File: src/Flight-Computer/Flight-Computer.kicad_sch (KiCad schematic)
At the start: 30 parts, among them J1 Jumper_NO, P8 3220-20-0200-00, U1 STM32H750VBTx, Y1 ECS-240-18-33-JGN-TR

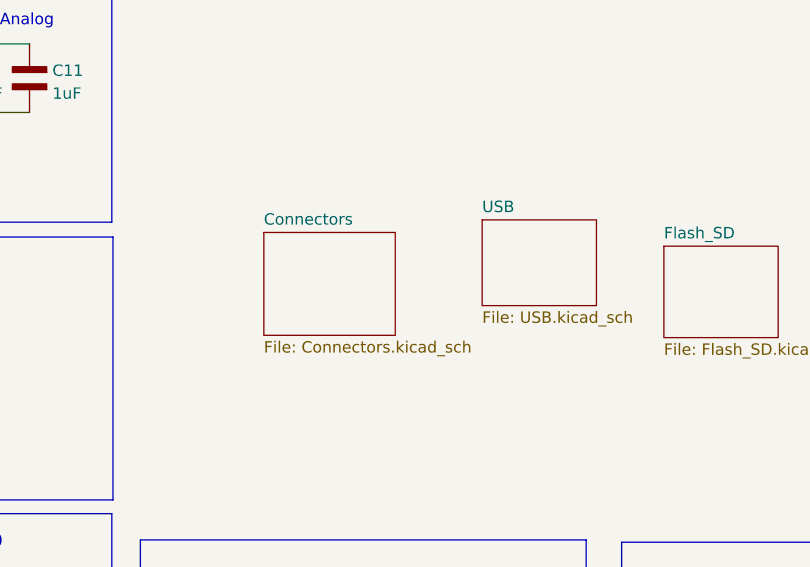
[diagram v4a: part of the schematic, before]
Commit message: deleted connector schematic sheet
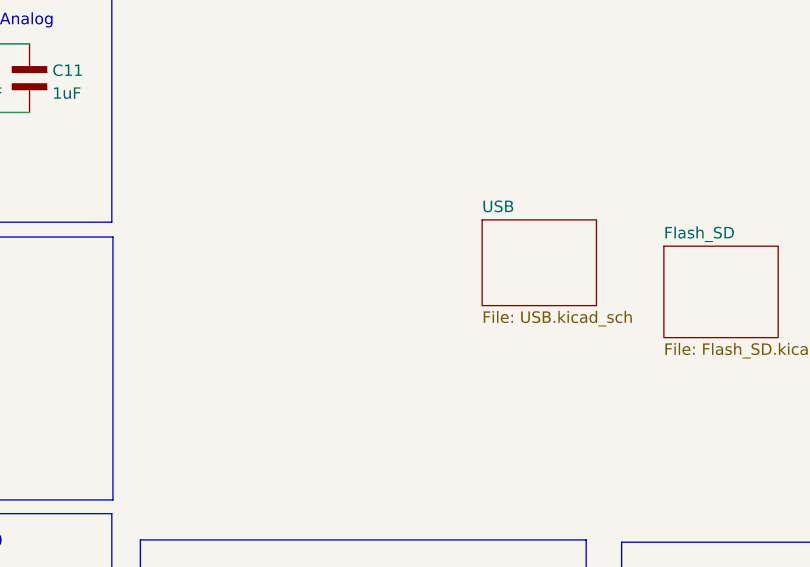
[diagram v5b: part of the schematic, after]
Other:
- removed sheet Connectors
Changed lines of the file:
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@@
-    )
-  )
-  (sheet (at 190.881 59.817) (size 14.605 11.43) (fields_autoplaced)
-    (stroke (width 0) (type solid) (color 0 0 0 0))
-    (fill (color 0 0 0 0.0000))
-    (property "Sheet name" "Connectors" (id 0) (at 190.881 59.1054 0)
-      (effects (font (size 1.27 1.27)) (justify left bottom))
-    )
-    (property "Sheet file" "Connectors.kicad_sch" (id 1) (at 190.881 71.8316 0)
-      (effects (font (size 1.27 1.27)) (justify left top))
     )
   )
@@
     (path "/" (page "1"))
     (path "/00000000-0000-0000-0000-00006177d07c" (page "3"))
-    (path "/00000000-0000-0000-0000-000060e24895" (page "4"))
     (path "/00000000-0000-0000-0000-000060daa9b3" (page "5"))
   )
@@
     (path "/00000000-0000-0000-0000-000060de602c"
       (reference "#PWR01") (unit 1) (value "Earth") (footprint "")
-    )
-    (path "/00000000-0000-0000-0000-000060e24895/00000000-0000-0000-0000-00006138d033"
-      (reference "#PWR02") (unit 1) (value "Earth") (footprint "")
     )
     (path "/00000000-0000-0000-0000-00006177d07c/00000000-0000-0000-0000-000061788b6e"
@@
     (path "/00000000-0000-0000-0000-00006177d07c/00000000-0000-0000-0000-0000617f979c"
       (reference "#PWR05") (unit 1) (value "Earth") (footprint "")
-    )
-    (path "/00000000-0000-0000-0000-000060e24895/00000000-0000-0000-0000-00006193d92b"
-      (reference "#PWR06") (unit 1) (value "Earth") (footprint "")
-    )
-    (path "/00000000-0000-0000-0000-000060e24895/00000000-0000-0000-0000-000061c08552"
-      (reference "#PWR07") (unit 1) (value "Earth") (footprint "")
     )
     (path "/08947480-7ace-467b-8a10-40dde61ef700"
@@
     (path "/00000000-0000-0000-0000-000060daa9b3/00000000-0000-0000-0000-000060fb3329"
       (reference "#PWR0110") (unit 1) (value "Earth") (footprint "")
-    )
-    (path "/00000000-0000-0000-0000-000060e24895/00000000-0000-0000-0000-000060dbde57"
-      (reference "#PWR0112") (unit 1) (value "Earth") (footprint "")
     )
     (path "/cea4c973-2fb2-41e2-9d5a-5ad0a7921ca6"
@@
       (reference "P2") (unit 1) (value "USB") (footprint "Engine-Controller:USB-TypeB")
     )
-    (path "/00000000-0000-0000-0000-000060e24895/00000000-0000-0000-0000-00006193d931"
-      (reference "P3") (unit 1) (value "SBH11-PBPC-D05-RA-BK") (footprint "Engine-Controller:SBH11-PBPC-D05-RA-BK")
-    )
-    (path "/00000000-0000-0000-0000-000060e24895/00000000-0000-0000-0000-000061252cb3"
-      (reference "P4") (unit 1) (value "0901471110") (footprint "Engine-Controller:0901471110")
-    )
-    (path "/00000000-0000-0000-0000-000060e24895/00000000-0000-0000-0000-000061255d75"
-      (reference "P5") (unit 1) (value "66953-005LF") (footprint "Engine-Controller:66953-005LF")
-    )
     (path "/00000000-0000-0000-0000-00006177d07c/00000000-0000-0000-0000-0000617f7ccb"
       (reference "P6") (unit 1) (value "Micro_SD_Card") (footprint "Engine-Controller:GCT_MEM2075-00-140-01-A")
-    )
-    (path "/00000000-0000-0000-0000-000060e24895/00000000-0000-0000-0000-000061bf9e85"
-      (reference "P7") (unit 1) (value "0901471110") (footprint "Engine-Controller:0901471110")
     )
     (path "/b101f496-de41-4d70-bd94-f188bbb0c195"
@@
       (reference "U1") (unit 1) (value "STM32H750VBTx") (footprint "Package_QFP:LQFP-100_14x14mm_P0.5mm")
     )
-    (path "/00000000-0000-0000-0000-000060e24895/00000000-0000-0000-0000-00006134c986"
-      (reference "U4") (unit 1) (value "SN74LV07ADR") (footprint "Engine-Controller:SN74LV07ADR")
-    )
     (path "/00000000-0000-0000-0000-00006177d07c/00000000-0000-0000-0000-0000617854ea"

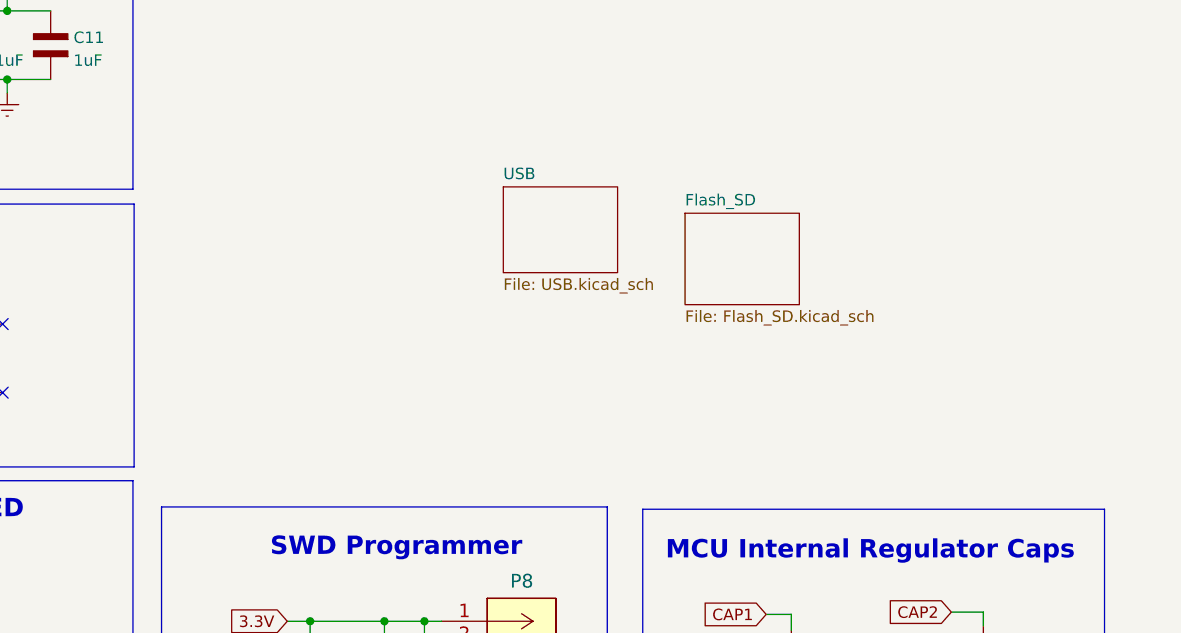
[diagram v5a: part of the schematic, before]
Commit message: added second sheet for peripheral functionality
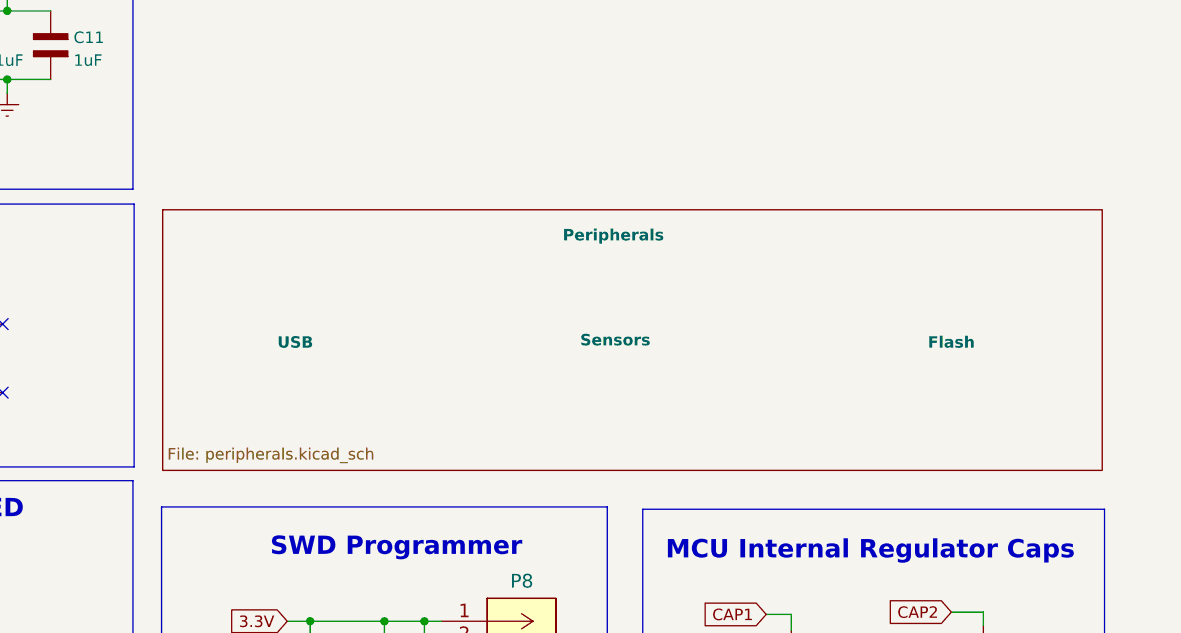
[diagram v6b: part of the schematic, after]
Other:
- removed sheet Flash_SD
- removed sheet USB
- added sheet Peripherals (peripherals.kicad_sch)
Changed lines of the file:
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@@
     (pin "2")
   )
-  (sheet (at 215.138 58.42) (size 12.7 9.525) (fields_autoplaced)
-    (stroke (width 0) (type solid) (color 0 0 0 0))
+  (sheet (at 177.292 60.96) (size 104.394 28.956)
+    (stroke (width 0.1524) (type solid) (color 0 0 0 0))
     (fill (color 0 0 0 0.0000))
-    (property "Sheet name" "USB" (id 0) (at 215.138 57.7084 0)
-      (effects (font (size 1.27 1.27)) (justify left bottom))
+    (property "Sheet name" "Peripherals" (id 0) (at 221.742 64.516 0)
+      (effects (font (size 1.27 1.27) bold) (justify left bottom))
     )
-    (property "Sheet file" "USB.kicad_sch" (id 1) (at 215.138 68.5296 0)
+    (property "Sheet file" "peripherals.kicad_sch" (id 1) (at 177.8 87.376 0)
       (effects (font (size 1.27 1.27)) (justify left top))
     )
-  )
-  (sheet (at 235.331 61.341) (size 12.7 10.16) (fields_autoplaced)
-    (stroke (width 0) (type solid) (color 0 0 0 0))
-    (fill (color 0 0 0 0.0000))
-    (property "Sheet name" "Flash_SD" (id 0) (at 235.331 60.6294 0)
-      (effects (font (size 1.27 1.27)) (justify left bottom))
+    (property "Field2" "USB" (id 2) (at 192.024 75.692 0)
+      (effects (font (size 1.27 1.27) bold))
     )
-    (property "Sheet file" "Flash_SD.kicad_sch" (id 1) (at 235.331 72.0856 0)
-      (effects (font (size 1.27 1.27)) (justify left top))
+    (property "Field3" "Flash" (id 3) (at 264.922 75.692 0)
+      (effects (font (size 1.27 1.27) bold))
+    )
+    (property "Field4" "Sensors" (id 4) (at 227.584 75.438 0)
+      (effects (font (size 1.27 1.27) bold))
     )
   )
   (sheet_instances
     (path "/" (page "1"))
-    (path "/00000000-0000-0000-0000-00006177d07c" (page "3"))
-    (path "/00000000-0000-0000-0000-000060daa9b3" (page "5"))
+    (path "/b65729ce-aade-4707-9cc1-eb9bb9e47e4f" (page "4"))
   )
   (symbol_instances
     (path "/00000000-0000-0000-0000-000060de602c"
       (reference "#PWR01") (unit 1) (value "Earth") (footprint "")
-    )
-    (path "/00000000-0000-0000-0000-00006177d07c/00000000-0000-0000-0000-000061788b6e"
-      (reference "#PWR03") (unit 1) (value "Earth") (footprint "")
-    )
-    (path "/00000000-0000-0000-0000-00006177d07c/00000000-0000-0000-0000-00006180735a"
-      (reference "#PWR04") (unit 1) (value "Earth") (footprint "")
-    )
-    (path "/00000000-0000-0000-0000-00006177d07c/00000000-0000-0000-0000-0000617f979c"
-      (reference "#PWR05") (unit 1) (value "Earth") (footprint "")
     )
     (path "/08947480-7ace-467b-8a10-40dde61ef700"
@@
     (path "/f0b9fa4a-3726-4357-8f1e-c3a8664a31ee"
       (reference "#PWR017") (unit 1) (value "Earth") (footprint "")
-    )
-    (path "/00000000-0000-0000-0000-000060daa9b3/00000000-0000-0000-0000-000060fb3329"
-      (reference "#PWR0110") (unit 1) (value "Earth") (footprint "")
     )
     (path "/cea4c973-2fb2-41e2-9d5a-5ad0a7921ca6"
@@
       (reference "LOGO1") (unit 1) (value "Logo") (footprint "")
     )
-    (path "/00000000-0000-0000-0000-000060daa9b3/00000000-0000-0000-0000-000061ddec99"
-      (reference "P2") (unit 1) (value "USB") (footprint "Engine-Controller:USB-TypeB")
-    )
-    (path "/00000000-0000-0000-0000-00006177d07c/00000000-0000-0000-0000-0000617f7ccb"
-      (reference "P6") (unit 1) (value "Micro_SD_Card") (footprint "Engine-Controller:GCT_MEM2075-00-140-01-A")
-    )
     (path "/b101f496-de41-4d70-bd94-f188bbb0c195"
       (reference "P8") (unit 1) (value "3220-20-0200-00") (footprint "CONN20_D10-RA-BK_SUL")
@@
       (reference "R6") (unit 1) (value "280") (footprint "")
     )
-    (path "/00000000-0000-0000-0000-00006177d07c/00000000-0000-0000-0000-0000618d69c9"
-      (reference "R7") (unit 1) (value "10k") (footprint "Engine-Controller:RES_0603")
-    )
     (path "/a77929a2-6f9e-4809-86d9-0b42c19c8063"
       (reference "R10") (unit 1) (value "100k") (footprint "")
@@
       (reference "TP1") (unit 1) (value "TP") (footprint "")
     )
-    (path "/00000000-0000-0000-0000-00006177d07c/00000000-0000-0000-0000-0000619d48b0"
-      (reference "TP6") (unit 1) (value "TP") (footprint "Engine-Controller:TP")
-    )
-    (path "/00000000-0000-0000-0000-00006177d07c/00000000-0000-0000-0000-0000619d6a4e"
-      (reference "TP7") (unit 1) (value "TP") (footprint "Engine-Controller:TP")
-    )
-    (path "/00000000-0000-0000-0000-00006177d07c/00000000-0000-0000-0000-0000619d874e"
-      (reference "TP8") (unit 1) (value "TP") (footprint "Engine-Controller:TP")
-    )
-    (path "/00000000-0000-0000-0000-00006177d07c/00000000-0000-0000-0000-0000619de8d4"
-      (reference "TP9") (unit 1) (value "TP") (footprint "Engine-Controller:TP")
-    )
     (path "/00000000-0000-0000-0000-0000614b51f2"
       (reference "U1") (unit 1) (value "STM32H750VBTx") (footprint "Package_QFP:LQFP-100_14x14mm_P0.5mm")
     )
-    (path "/00000000-0000-0000-0000-00006177d07c/00000000-0000-0000-0000-0000617854ea"
-      (reference "U5") (unit 1) (value "SST25VF040B-50-4I-S2AE-T") (footprint "Engine-Controller:SST25VF040B-50-4I-S2AE-T")
-    )
     (path "/4fe127d3-8d94-46ea-90c9-64f19144e6e4"
